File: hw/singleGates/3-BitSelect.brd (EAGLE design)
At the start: 36 parts, among them Q1 BC817, Q10 BC817, Q11 BC817, Q12 BC817, Q13 BC817, Q14 BC817, Q15 BC817, Q16 BC817, Q17 BC817, Q2 BC817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

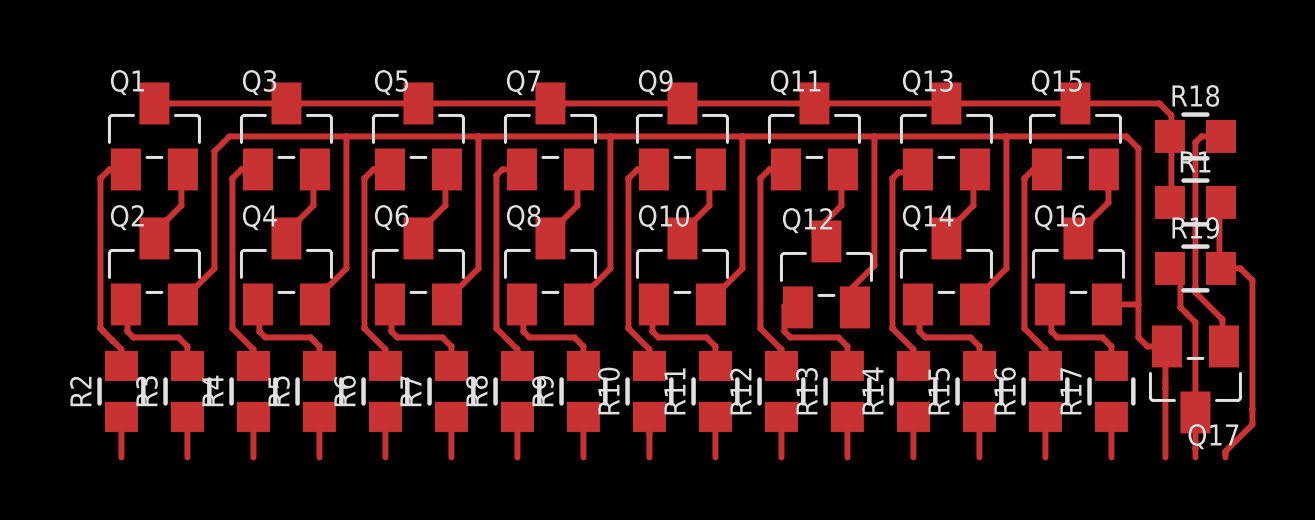
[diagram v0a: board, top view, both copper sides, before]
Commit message: Trying to mimize gates some more
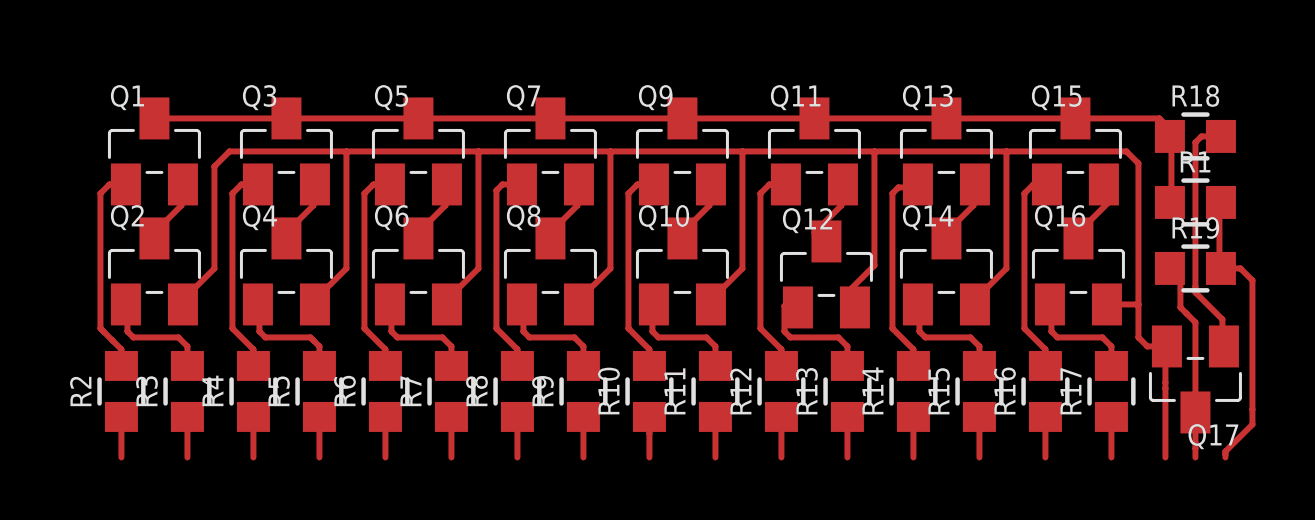
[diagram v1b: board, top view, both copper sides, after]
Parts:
- moved Q1 0.50 mm to (2.30, 10.2)
- moved Q11 0.50 mm to (24.3, 10.2)
- moved Q13 0.50 mm to (28.7, 10.2)
- moved Q15 0.50 mm to (33.0, 10.2)
- moved Q3 0.50 mm to (6.70, 10.2)
- moved Q5 0.50 mm to (11.1, 10.2)
- moved Q7 0.50 mm to (15.5, 10.2)
- moved Q9 0.50 mm to (19.9, 10.2)
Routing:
- net _VN: track 85.7 -> 81.7 mm
- net SEL_INT: track 37.1 -> 36.6 mm
- net N$52: track 2.82 -> 2.32 mm
- net N$50: track 7.41 -> 6.91 mm
- net N$49: track 2.69 -> 2.19 mm
- net N$47: track 7.51 -> 7.01 mm
- net N$46: track 2.99 -> 2.49 mm
- net N$44: track 7.51 -> 7.01 mm
- net N$43: track 2.69 -> 2.19 mm
- net N$41: track 7.51 -> 7.01 mm
- net N$40: track 2.69 -> 2.19 mm
- net N$38: track 7.57 -> 7.07 mm
- net N$37: track 2.69 -> 2.19 mm
- net N$35: track 7.51 -> 7.01 mm
- net N$34: track 2.69 -> 2.19 mm
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
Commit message: fixes some offset and juction issues
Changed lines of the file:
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@@
 <?xml version="1.0" encoding="utf-8"?>
 <!DOCTYPE eagle SYSTEM "eagle.dtd">
-<eagle version="7.3.0">
+<eagle version="7.4.0">
 <drawing>
 <settings>
@@
 <wire x1="26.3" y1="10.2" x2="30.7" y2="10.2" width="0.2" layer="1"/>
 <wire x1="30.7" y1="10.2" x2="34.7" y2="10.2" width="0.2" layer="1"/>
-<wire x1="7.65" y1="5.1" x2="7.65" y2="5.15" width="0.2" layer="1"/>
 <wire x1="7.65" y1="5.15" x2="7.7" y2="5.2" width="0.2" layer="1"/>
 <wire x1="7.7" y1="5.2" x2="7.7" y2="5.3" width="0.2" layer="1"/>
@@
 <wire x1="36" y1="3.65" x2="36.05" y2="3.7" width="0.2" layer="1"/>
 <contactref element="Q2" pad="P$2"/>
-<contactref element="Q4" pad="P$2"/>
 <contactref element="Q6" pad="P$2"/>
 <contactref element="Q8" pad="P$2"/>
@@
 <contactref element="Q16" pad="P$2"/>
 <contactref element="Q17" pad="P$2"/>
+<contactref element="Q4" pad="P$2"/>
 <wire x1="20.9" y1="5.1" x2="20.85" y2="5.1" width="0" layer="19" extent="1-1"/>
+<wire x1="7.65" y1="5.1" x2="7.65" y2="5.15" width="0" layer="19" extent="1-1"/>
 </signal>
 <signal name="_VP">
